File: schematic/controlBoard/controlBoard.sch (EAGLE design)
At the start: 37 parts, among them IC2 DS3231/SO, IC3 LM1117MP-3.3, T1 BC547, T2 BC547, Y1 12MHz

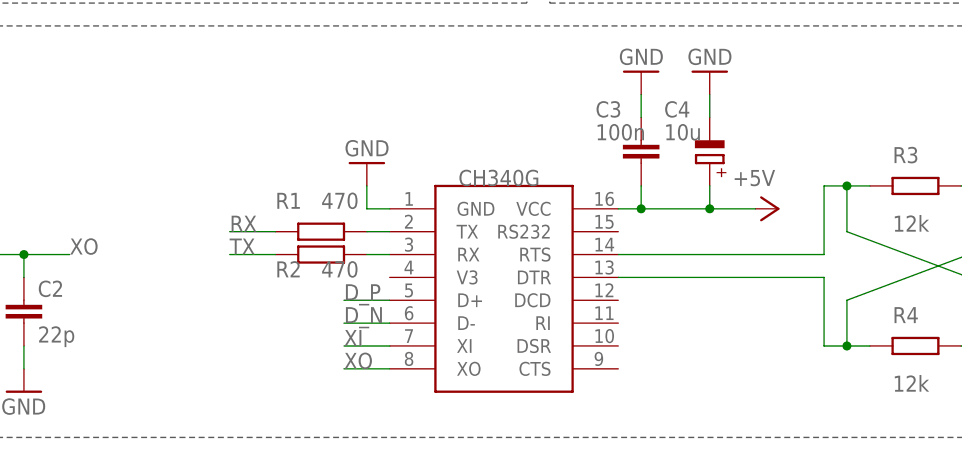
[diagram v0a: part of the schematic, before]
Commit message: Supply CH340 with 3V3 to fix ESP programming issue
In order to properly communicate with ESP it is required to use CH340
USB to serial in 3V3 mode.
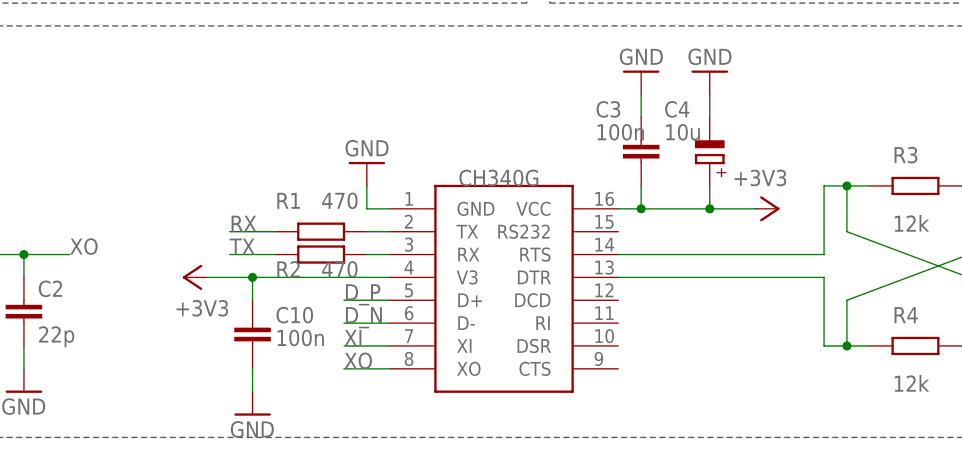
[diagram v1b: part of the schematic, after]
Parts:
- added C10: 100n, resistor:C-EUC0603
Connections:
- net +3V3: now also C10.1, C3.2, C4.+, U$2.V3, U$2.VCC
- net +5V: no longer C3.2, C4.+, U$2.VCC
- net GND: now also C10.2
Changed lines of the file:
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@@
 <part name="R2" library="resistor" library_urn="urn:adsk.eagle:library:348" deviceset="R-EU_" device="R0603" package3d_urn="urn:adsk.eagle:package:26057/1" value="470"/>
 <part name="GND9" library="supply1" library_urn="urn:adsk.eagle:library:371" deviceset="GND" device=""/>
-<part name="P+3" library="supply1" library_urn="urn:adsk.eagle:library:371" deviceset="+5V" device=""/>
 <part name="C3" library="resistor" library_urn="urn:adsk.eagle:library:348" deviceset="C-EU" device="C0603" package3d_urn="urn:adsk.eagle:package:26138/1" value="100n"/>
 <part name="GND10" library="supply1" library_urn="urn:adsk.eagle:library:371" deviceset="GND" device=""/>
@@
 <part name="R12" library="resistor" library_urn="urn:adsk.eagle:library:348" deviceset="R-EU_" device="R0603" package3d_urn="urn:adsk.eagle:package:26057/1" value="4k7"/>
 <part name="+3V8" library="supply1" library_urn="urn:adsk.eagle:library:371" deviceset="+3V3" device=""/>
+<part name="+3V9" library="supply1" library_urn="urn:adsk.eagle:library:371" deviceset="+3V3" device=""/>
+<part name="+3V10" library="supply1" library_urn="urn:adsk.eagle:library:371" deviceset="+3V3" device=""/>
+<part name="C10" library="resistor" library_urn="urn:adsk.eagle:library:348" deviceset="C-EU" device="C0603" package3d_urn="urn:adsk.eagle:package:26138/1" value="100n"/>
+<part name="GND2" library="supply1" library_urn="urn:adsk.eagle:library:371" deviceset="GND" device=""/>
 </parts>
 <sheets>
@@
 <attribute name="VALUE" x="111.76" y="33.02" size="1.778" layer="96" rot="R180"/>
 </instance>
-<instance part="P+3" gate="1" x="154.94" y="25.4" smashed="yes" rot="R270">
-<attribute name="VALUE" x="149.86" y="27.94" size="1.778" layer="96"/>
-</instance>
 <instance part="C3" gate="G$1" x="139.7" y="33.02" smashed="yes">
 <attribute name="NAME" x="134.62" y="35.56" size="1.778" layer="95"/>
@@
 <instance part="+3V8" gate="G$1" x="144.78" y="101.6" smashed="yes">
 <attribute name="VALUE" x="142.24" y="101.6" size="1.778" layer="96"/>
+</instance>
+<instance part="+3V9" gate="G$1" x="154.94" y="25.4" smashed="yes" rot="R270">
+<attribute name="VALUE" x="149.86" y="27.94" size="1.778" layer="96"/>
+</instance>
+<instance part="+3V10" gate="G$1" x="88.9" y="17.78" smashed="yes" rot="R90">
+<attribute name="VALUE" x="93.98" y="15.24" size="1.778" layer="96" rot="R180"/>
+</instance>
+<instance part="C10" gate="G$1" x="96.52" y="12.7" smashed="yes">
+<attribute name="NAME" x="99.06" y="12.7" size="1.778" layer="95"/>
+<attribute name="VALUE" x="99.06" y="10.16" size="1.778" layer="96"/>
+</instance>
+<instance part="GND2" gate="1" x="96.52" y="2.54" smashed="yes">
+<attribute name="VALUE" x="93.98" y="0" size="1.778" layer="96"/>
 </instance>
 </instances>
@@
 <wire x1="167.64" y1="119.38" x2="167.64" y2="127" width="0.1524" layer="91"/>
 </segment>
+<segment>
+<pinref part="GND2" gate="1" pin="GND"/>
+<pinref part="C10" gate="G$1" pin="2"/>
+<wire x1="96.52" y1="5.08" x2="96.52" y2="7.62" width="0.1524" layer="91"/>
+</segment>
 </net>
 <net name="+5V" class="0">
-<segment>
-<pinref part="U$2" gate="G$1" pin="VCC"/>
-<pinref part="P+3" gate="1" pin="+5V"/>
-<wire x1="152.4" y1="25.4" x2="147.32" y2="25.4" width="0.1524" layer="91"/>
-<pinref part="C3" gate="G$1" pin="2"/>
-<wire x1="147.32" y1="25.4" x2="139.7" y2="25.4" width="0.1524" layer="91"/>
-<wire x1="139.7" y1="25.4" x2="137.16" y2="25.4" width="0.1524" layer="91"/>
-<wire x1="139.7" y1="27.94" x2="139.7" y2="25.4" width="0.1524" layer="91"/>
-<junction x="139.7" y="25.4"/>
-<pinref part="C4" gate="G$1" pin="+"/>
-<wire x1="147.32" y1="27.94" x2="147.32" y2="25.4" width="0.1524" layer="91"/>
-<junction x="147.32" y="25.4"/>
-</segment>
 <segment>
 <pinref part="P+4" gate="1" pin="+5V"/>
@@
 <wire x1="144.78" y1="96.52" x2="144.78" y2="99.06" width="0.1524" layer="91"/>
 </segment>
-</net>
+<segment>
+<pinref part="U$2" gate="G$1" pin="VCC"/>
+<wire x1="152.4" y1="25.4" x2="147.32" y2="25.4" width="0.1524" layer="91"/>
+<pinref part="C3" gate="G$1" pin="2"/>
+<wire x1="147.32" y1="25.4" x2="139.7" y2="25.4" width="0.1524" layer="91"/>
+<wire x1="139.7" y1="25.4" x2="137.16" y2="25.4" width="0.1524" layer="91"/>
+<wire x1="139.7" y1="27.94" x2="139.7" y2="25.4" width="0.1524" layer="91"/>
+<junction x="139.7" y="25.4"/>
+<pinref part="C4" gate="G$1" pin="+"/>
+<wire x1="147.32" y1="27.94" x2="147.32" y2="25.4" width="0.1524" layer="91"/>
+<junction x="147.32" y="25.4"/>
+<pinref part="+3V9" gate="G$1" pin="+3V3"/>
+</segment>
+<segment>
+<pinref part="U$2" gate="G$1" pin="V3"/>
+<pinref part="+3V10" gate="G$1" pin="+3V3"/>
+<wire x1="111.76" y1="17.78" x2="96.52" y2="17.78" width="0.1524" layer="91"/>
+<pinref part="C10" gate="G$1" pin="1"/>
+<wire x1="96.52" y1="17.78" x2="91.44" y2="17.78" width="0.1524" layer="91"/>
+<wire x1="96.52" y1="15.24" x2="96.52" y2="17.78" width="0.1524" layer="91"/>
+<junction x="96.52" y="17.78"/>
+</segment>
+</net>

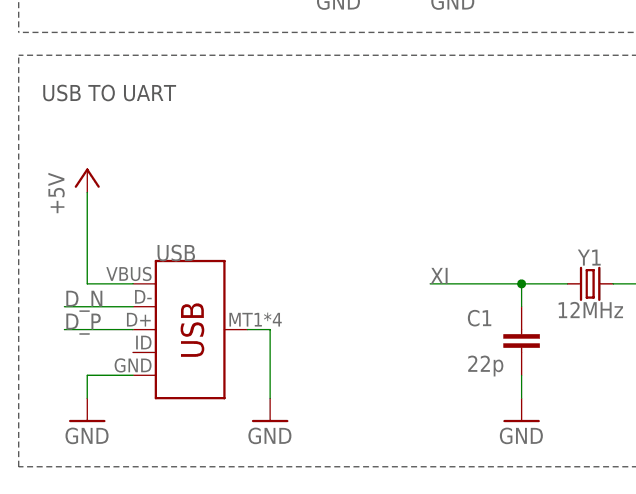
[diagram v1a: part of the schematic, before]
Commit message: Add ESD protection to USB data lanes
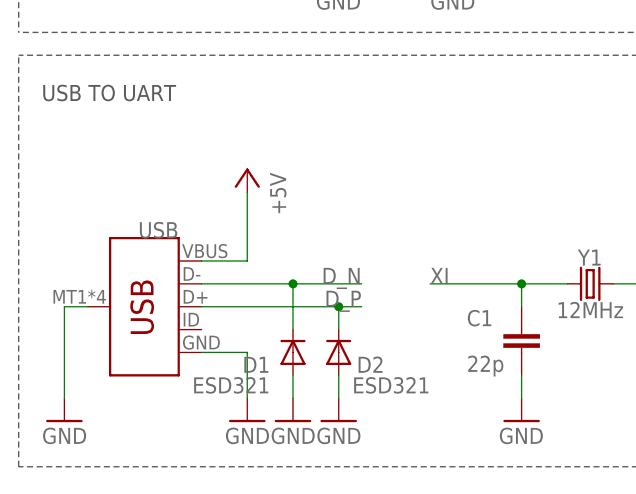
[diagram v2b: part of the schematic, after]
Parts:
- added D1, D2: ESD321, diode:DIODE-SOD523
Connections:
- net D_N: now also D1.C
- net D_P: now also D2.C
- net GND: now also D1.A, D2.A
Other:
- moved on the sheet: USB
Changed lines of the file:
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@@
 <part name="C10" library="resistor" library_urn="urn:adsk.eagle:library:348" deviceset="C-EU" device="C0603" package3d_urn="urn:adsk.eagle:package:26138/1" value="100n"/>
 <part name="GND2" library="supply1" library_urn="urn:adsk.eagle:library:371" deviceset="GND" device=""/>
+<part name="D1" library="diode" library_urn="urn:adsk.eagle:library:210" deviceset="DIODE-" device="SOD523" package3d_urn="urn:adsk.eagle:package:43410/1" value="ESD321"/>
+<part name="D2" library="diode" library_urn="urn:adsk.eagle:library:210" deviceset="DIODE-" device="SOD523" package3d_urn="urn:adsk.eagle:package:43410/1" value="ESD321"/>
+<part name="GND3" library="supply1" library_urn="urn:adsk.eagle:library:371" deviceset="GND" device=""/>
+<part name="GND4" library="supply1" library_urn="urn:adsk.eagle:library:371" deviceset="GND" device=""/>
 </parts>
 <sheets>
@@
 <attribute name="VALUE" x="185.42" y="10.16" size="1.778" layer="96" rot="MR180"/>
 </instance>
-<instance part="USB" gate="G$1" x="17.78" y="15.24" smashed="yes">
-<attribute name="VALUE" x="15.24" y="7.366" size="1.778" layer="96" font="vector" align="top-left"/>
-<attribute name="NAME" x="15.24" y="22.86" size="1.778" layer="95" font="vector"/>
-</instance>
-<instance part="GND14" gate="1" x="7.62" y="5.08" smashed="yes">
-<attribute name="VALUE" x="5.08" y="2.54" size="1.778" layer="96"/>
-</instance>
-<instance part="GND15" gate="1" x="27.94" y="5.08" smashed="yes">
-<attribute name="VALUE" x="25.4" y="2.54" size="1.778" layer="96"/>
-</instance>
-<instance part="P+4" gate="1" x="7.62" y="33.02" smashed="yes">
-<attribute name="VALUE" x="5.08" y="27.94" size="1.778" layer="96" rot="R90"/>
+<instance part="USB" gate="G$1" x="15.24" y="17.78" smashed="yes" rot="MR0">
+<attribute name="VALUE" x="17.78" y="9.906" size="1.778" layer="96" font="vector" rot="MR0" align="top-left"/>
+<attribute name="NAME" x="17.78" y="25.4" size="1.778" layer="95" font="vector" rot="MR0"/>
+</instance>
+<instance part="GND14" gate="1" x="25.4" y="5.08" smashed="yes" rot="MR0">
+<attribute name="VALUE" x="27.94" y="2.54" size="1.778" layer="96" rot="MR0"/>
+</instance>
+<instance part="GND15" gate="1" x="5.08" y="5.08" smashed="yes" rot="MR0">
+<attribute name="VALUE" x="7.62" y="2.54" size="1.778" layer="96" rot="MR0"/>
+</instance>
+<instance part="P+4" gate="1" x="25.4" y="33.02" smashed="yes" rot="MR0">
+<attribute name="VALUE" x="27.94" y="27.94" size="1.778" layer="96" rot="MR90"/>
 </instance>
 <instance part="R5" gate="G$1" x="15.24" y="86.36" smashed="yes" rot="R180">
@@
 <instance part="GND2" gate="1" x="96.52" y="2.54" smashed="yes">
 <attribute name="VALUE" x="93.98" y="0" size="1.778" layer="96"/>
+</instance>
+<instance part="D1" gate="G$1" x="30.48" y="12.7" smashed="yes" rot="R90">
+<attribute name="NAME" x="27.94" y="12.2174" size="1.778" layer="95" rot="R180"/>
+<attribute name="VALUE" x="27.94" y="9.9314" size="1.778" layer="96" rot="R180"/>
+</instance>
+<instance part="D2" gate="G$1" x="35.56" y="12.7" smashed="yes" rot="R90">
+<attribute name="NAME" x="40.64" y="12.2174" size="1.778" layer="95" rot="R180"/>
+<attribute name="VALUE" x="45.72" y="9.9314" size="1.778" layer="96" rot="R180"/>
+</instance>
+<instance part="GND3" gate="1" x="30.48" y="5.08" smashed="yes" rot="MR0">
+<attribute name="VALUE" x="33.02" y="2.54" size="1.778" layer="96" rot="MR0"/>
+</instance>
+<instance part="GND4" gate="1" x="35.56" y="5.08" smashed="yes" rot="MR0">
+<attribute name="VALUE" x="38.1" y="2.54" size="1.778" layer="96" rot="MR0"/>
 </instance>
 </instances>
@@
 <pinref part="USB" gate="G$1" pin="GND"/>
 <pinref part="GND14" gate="1" pin="GND"/>
-<wire x1="12.7" y1="10.16" x2="7.62" y2="10.16" width="0.1524" layer="91"/>
-<wire x1="7.62" y1="10.16" x2="7.62" y2="7.62" width="0.1524" layer="91"/>
+<wire x1="20.32" y1="12.7" x2="25.4" y2="12.7" width="0.1524" layer="91"/>
+<wire x1="25.4" y1="12.7" x2="25.4" y2="7.62" width="0.1524" layer="91"/>
 </segment>
 <segment>
 <pinref part="USB" gate="G$1" pin="SHIELD"/>
 <pinref part="GND15" gate="1" pin="GND"/>
-<wire x1="25.4" y1="15.24" x2="27.94" y2="15.24" width="0.1524" layer="91"/>
-<wire x1="27.94" y1="15.24" x2="27.94" y2="7.62" width="0.1524" layer="91"/>
+<wire x1="7.62" y1="17.78" x2="5.08" y2="17.78" width="0.1524" layer="91"/>
+<wire x1="5.08" y1="17.78" x2="5.08" y2="7.62" width="0.1524" layer="91"/>
 </segment>
 <segment>
@@
 <wire x1="96.52" y1="5.08" x2="96.52" y2="7.62" width="0.1524" layer="91"/>
 </segment>
+<segment>
+<pinref part="GND3" gate="1" pin="GND"/>
+<pinref part="D1" gate="G$1" pin="A"/>
+<wire x1="30.48" y1="7.62" x2="30.48" y2="10.16" width="0.1524" layer="91"/>
+</segment>
+<segment>
+<pinref part="GND4" gate="1" pin="GND"/>
+<pinref part="D2" gate="G$1" pin="A"/>
+<wire x1="35.56" y1="7.62" x2="35.56" y2="10.16" width="0.1524" layer="91"/>
+</segment>
 </net>
 <net name="+5V" class="0">
@@
 <pinref part="P+4" gate="1" pin="+5V"/>
 <pinref part="USB" gate="G$1" pin="VBUS"/>
-<wire x1="12.7" y1="20.32" x2="7.62" y2="20.32" width="0.1524" layer="91"/>
-<wire x1="7.62" y1="20.32" x2="7.62" y2="30.48" width="0.1524" layer="91"/>
+<wire x1="20.32" y1="22.86" x2="25.4" y2="22.86" width="0.1524" layer="91"/>
+<wire x1="25.4" y1="22.86" x2="25.4" y2="30.48" width="0.1524" layer="91"/>
 </segment>
 <segment>
@@
 <segment>
 <pinref part="USB" gate="G$1" pin="D-"/>
-<wire x1="12.7" y1="17.78" x2="5.08" y2="17.78" width="0.1524" layer="91"/>
-<label x="5.08" y="17.78" size="1.778" layer="95"/>
+<wire x1="20.32" y1="20.32" x2="30.48" y2="20.32" width="0.1524" layer="91"/>
+<label x="38.1" y="20.32" size="1.778" layer="95" rot="MR0"/>
+<pinref part="D1" gate="G$1" pin="C"/>
+<wire x1="30.48" y1="20.32" x2="38.1" y2="20.32" width="0.1524" layer="91"/>
+<wire x1="30.48" y1="15.24" x2="30.48" y2="20.32" width="0.1524" layer="91"/>
+<junction x="30.48" y="20.32"/>
 </segment>
 </net>
@@
 <segment>
 <pinref part="USB" gate="G$1" pin="D+"/>
-<wire x1="12.7" y1="15.24" x2="5.08" y2="15.24" width="0.1524" layer="91"/>
-<label x="5.08" y="15.24" size="1.778" layer="95"/>
-</segment>
-</net>
+<wire x1="20.32" y1="17.78" x2="35.56" y2="17.78" width="0.1524" layer="91"/>
+<label x="38.1" y="17.78" size="1.778" layer="95" rot="MR0"/>
+<pinref part="D2" gate="G$1" pin="C"/>
+<wire x1="35.56" y1="17.78" x2="38.1" y2="17.78" width="0.1524" layer="91"/>
+<wire x1="35.56" y1="15.24" x2="35.56" y2="17.78" width="0.1524" layer="91"/>
+<junction x="35.56" y="17.78"/>
+</segment>
+</net>
